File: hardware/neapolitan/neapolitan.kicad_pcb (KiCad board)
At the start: 4 copper layers, 120 x 75 mm, 250 parts, among them J1 USB-MICRO-B, J10 GND_CLIP, J2 RF-SHIELD-FRAME, J3 RF-SHIELD-COVER, J4 MOUNTING_HOLE, J5 MOUNTING_HOLE, J6 MOUNTING_HOLE, J7 MOUNTING_HOLE, J8 MOUNTING_HOLE, J9 MOUNTING_HOLE, P13 GPO1, P14 XCVR_CLKOUT, P15 INTR, P16 CLKIN, P17 GPO6, P18 OEB, P19 GPO3, P2 CLKOUT, P20 GPIO, P21 REF_IN, P22 I2S, P27 MIXER_SDATA, P28 SD, P30 BANK2_AUX, P31 MIXER_SCLK, P32 MIXER_ENX, P33 MIXER_RESETX, P34 MIX_BYPASS, P35 !MIX_BYPASS, P36 VAA, P37 SCL, P38 SDA, P39 SSP1_SCK, P4 ANTENNA, P40 SSP1_MOSI, P41 SSP1_MISO, P42 TX, P43 RX, P44 HP, P45 LP, P46 TX_MIX_BP, P47 RX_MIX_BP, P48 TX_AMP, P49 RX_AMP, P5 LEDS, P50 AMP_BYPASS, P51 !TX_AMP_PWR, P52 !RX_AMP_PWR, P53 CS_XCVR, P55 TXENABLE, P56 RXENABLE, P57 XTAL2, P6 GPO4, P67 RSSI, P7 GPO2, P80 SHIELD, P83 GND, P84 GND, P85 GND, P86 GND, P87 GND, P88 GND, P89 GND, P9 BASEBAND, P90 GND, P91 GND, P92 GND, Q1 MOSFET_P, Q2 MOSFET_P, Q3 MOSFET_P, Q4 MOSFET_P, T1 MIX_IN_BALUN, T2 MIX_OUT_BALUN, T3 RX_BALUN, T4 TX_BALUN, U1 SKY13350, U10 SKY13350, U11 SKY13350, U12 SKY13317, U13 MGA-81563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

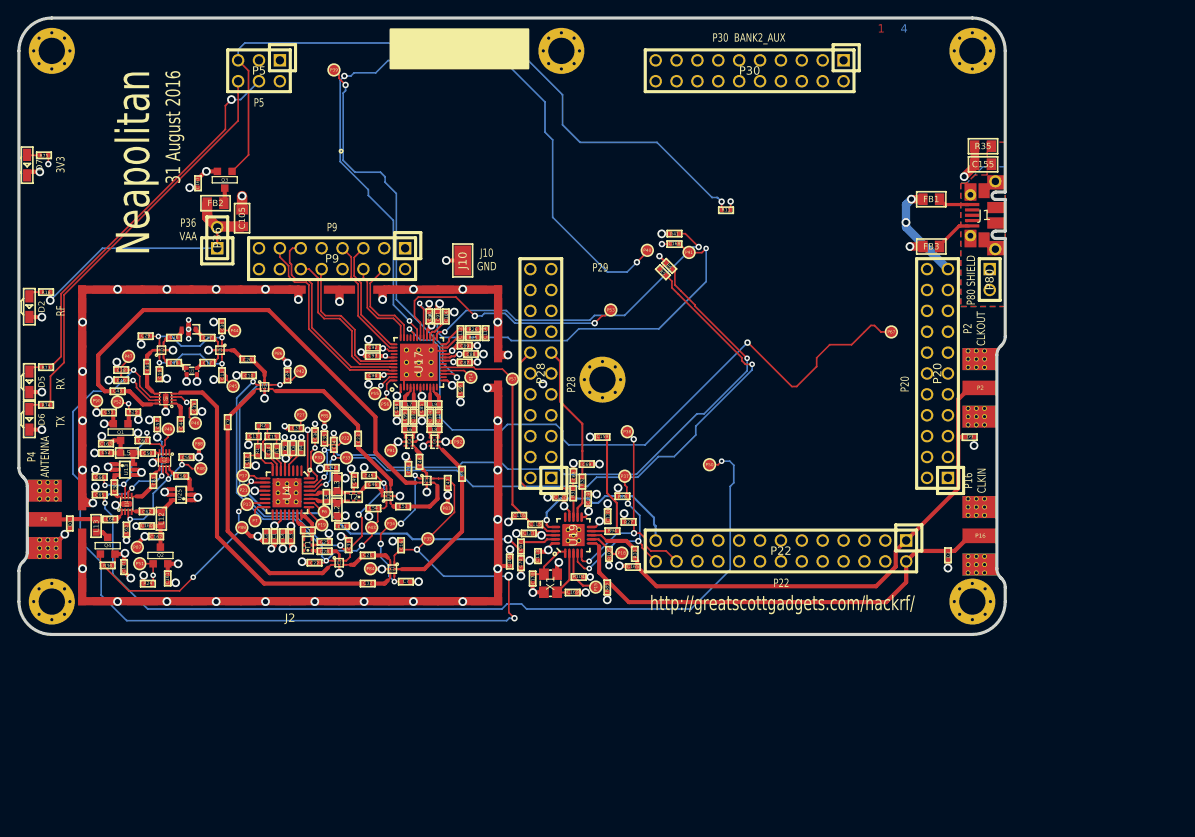
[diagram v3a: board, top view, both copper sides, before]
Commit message: Neapolitan: header pin assignments
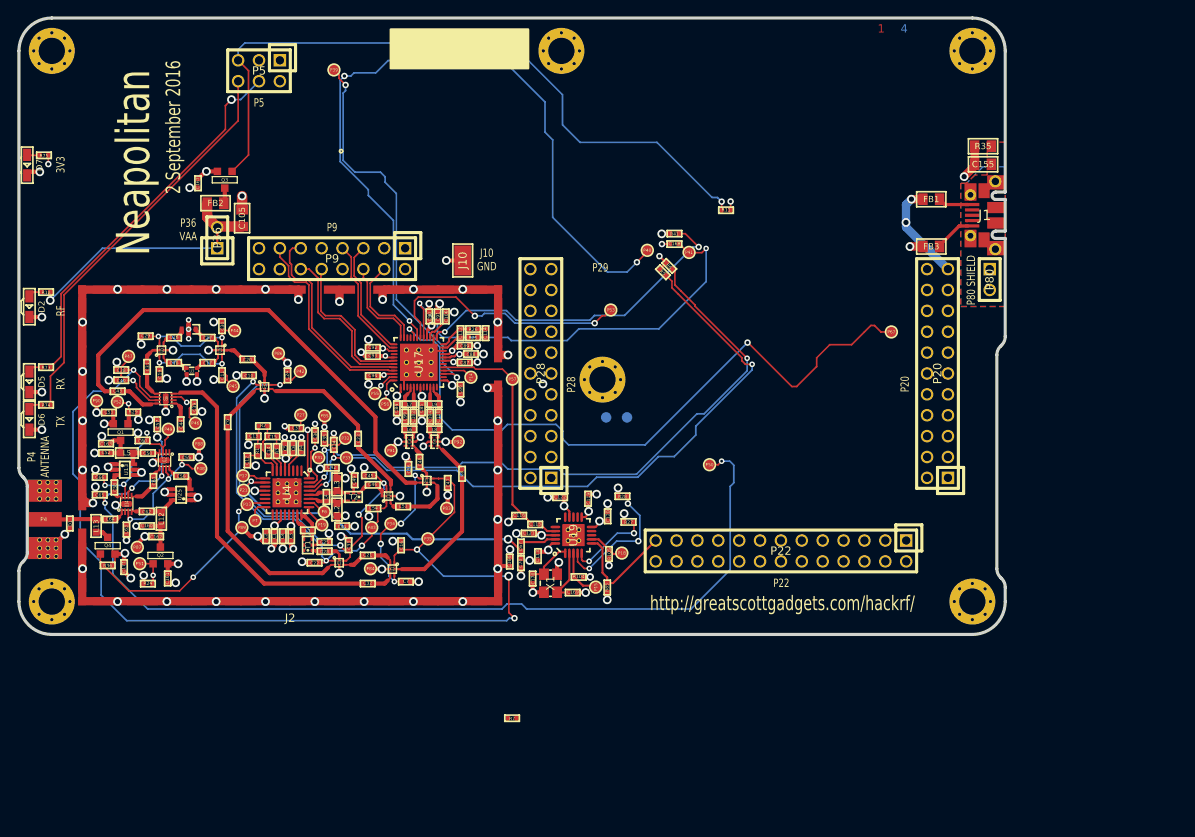
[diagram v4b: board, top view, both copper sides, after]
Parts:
- removed C159, C165, C68, C69: 100pF, hackrf:GSG-0402
- removed D3, D9: GSG-DIODE-TVS-BI, hackrf:GSG-0402
- removed P16: CLKIN, hackrf:GSG-SMA-73251-2120
- removed P2: CLKOUT, hackrf:GSG-SMA-73251-2120
- removed P30: BANK2_AUX, hackrf:GSG-HEADER-2x10
- removed R31, R32, R33, R94: 39, hackrf:GSG-0402
- added R7: 470, hackrf:GSG-0402, F.Cu at (120.0, 185.2)
- P37, P38: moved to B.Cu
- P39: value SSP1_SCK -> SSP0_SCK
- P40: value SSP1_MOSI -> SSP0_MOSI
- P41: value SSP1_MISO -> SSP0_MISO
- moved P37 7.51 mm to (131.4, 148.6)
- moved P38 1.75 mm to (134.0, 148.6)
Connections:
- C168 pad 1: SSP1_MISO -> (no net)
- P20 pad 17: (no net) -> /mcu/usb/power/VBUSCTRL
- P20 pad 18: (no net) -> RSSI
- P22 pad 1: CLKOUT -> (no net)
- P22 pad 2: CLKIN -> (no net)
- P22 pad 5: (no net) -> I2C1_SCL
- P22 pad 6: (no net) -> I2C1_SDA
- P22 pad 7: (no net) -> SSP0_MISO
- P22 pad 8: (no net) -> SSP0_SCK
- P22 pad 9: (no net) -> SSP0_MOSI
- P28 pad 10: (no net) -> XCVR_EN
- P28 pad 13: GCK2 -> (no net)
- P28 pad 14: GCK1 -> (no net)
- P28 pad 4: (no net) -> MIXER_ENX
- P28 pad 5: (no net) -> MIXER_SCLK
- P28 pad 6: (no net) -> MIXER_SDATA
- P28 pad 7: (no net) -> RXENABLE
- P28 pad 8: (no net) -> TXENABLE
- P28 pad 9: (no net) -> CS_XCVR
- P39 pad 1: SSP1_SCK -> SSP0_SCK
- P40 pad 1: SSP1_MOSI -> SSP0_MOSI
- P41 pad 1: SSP1_MISO -> SSP0_MISO
- R27 pad 2: SDA -> I2C1_SDA
- R28 pad 2: SCL -> I2C1_SCL
- R85 pad 1: CLKIN -> CLK6
- U17 pad 15: SSP1_SCK -> SSP0_SCK
- U17 pad 29: SSP1_MISO -> SSP0_MISO
- U17 pad 31: SSP1_MOSI -> SSP0_MOSI
- U19 pad 12: /baseband/CLK1 -> (no net)
- U19 pad 13: /baseband/CLK0 -> (no net)
- U19 pad 16: CLK6 -> (no net)
- U19 pad 4: SCL -> I2C1_SCL
- U19 pad 5: SDA -> I2C1_SDA
- U19 pad 6: CLKIN -> CLK6
- U19 pad 8: /baseband/CLK3 -> (no net)
- U19 pad 9: /baseband/CLK2 -> (no net)
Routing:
- net SSP1_MOSI: track 93.1 -> 0.00 mm, vias 3 -> 0
- net SSP0_MOSI: track 0.00 -> 93.1 mm, vias 0 -> 3
- net CLKOUT: track 62.2 -> 0.00 mm
- net CLKIN: track 58.6 -> 0.00 mm
- net SSP1_MISO: track 52.8 -> 0.00 mm, vias 2 -> 0
- net SSP0_MISO: track 0.00 -> 52.8 mm, vias 0 -> 2
- net SSP1_SCK: track 47.5 -> 0.00 mm, vias 2 -> 0
- net SSP0_SCK: track 0.00 -> 47.5 mm, vias 0 -> 2
- net SDA: track 28.6 -> 0.00 mm, vias 3 -> 0
- net GCK1: track 24.1 -> 0.00 mm
- net SCL: track 22.2 -> 0.00 mm, vias 3 -> 0
- net GCK2: track 16.7 -> 0.00 mm
- net I2C1_SCL: track 0.00 -> 16.3 mm, vias 0 -> 3
- net SGPIO_CLK: track 12.0 -> 0.00 mm
- net I2C1_SDA: track 0.00 -> 10.3 mm, vias 0 -> 2
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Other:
- board text added: "2 September 2016"
- board text removed: "31 August 2016"
- board text removed: "P16 CLKIN"
- board text removed: "P2 CLKOUT"
- board text removed: "P30 BANK2_AUX"

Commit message: Neapolitan: added I/O expander
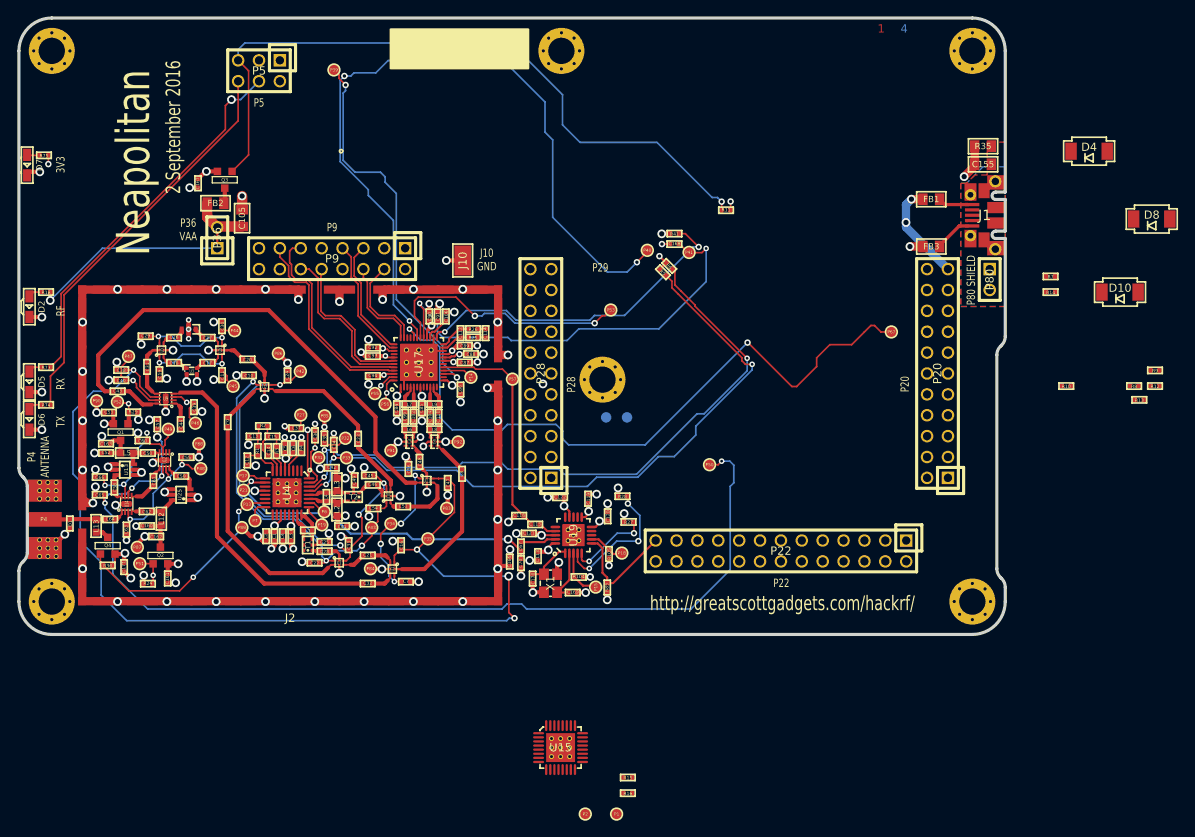
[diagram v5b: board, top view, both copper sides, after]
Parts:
- added D10: VIN_DIODE, gsg-modules:SOD128, F.Cu at (194.0, 133.3)
- added D4: BARREL_DIODE, gsg-modules:SOD128, F.Cu at (190.2, 116.2)
- added D8: VBUS2_DIODE, gsg-modules:SOD128, F.Cu at (197.8, 124.5)
- added P1: !IO_INT, hackrf:GSG-TESTPOINT-50MIL, F.Cu at (132.7, 196.8)
- added P2: !IO_RESET, hackrf:GSG-TESTPOINT-50MIL, F.Cu at (128.9, 196.8)
- added R10: 10k, hackrf:GSG-0402, F.Cu at (187.4, 144.8)
- added R12: 18k, hackrf:GSG-0402, F.Cu at (198.2, 144.8)
- added R13: 10k, hackrf:GSG-0402, F.Cu at (196.3, 146.5)
- added R14: 18k, hackrf:GSG-0402, F.Cu at (185.5, 133.3)
- added R15: 10k, hackrf:GSG-0402, F.Cu at (134.1, 192.4)
- added R16: 10k, hackrf:GSG-0402, F.Cu at (134.1, 194.3)
- added R8: 10k, hackrf:GSG-0402, F.Cu at (195.7, 144.8)
- added R9: 18k, hackrf:GSG-0402, F.Cu at (198.2, 142.9)
- added U15: TCA6424A, gsg-modules:QFN32-5, F.Cu at (125.9, 188.8)
- moved R7 84.7 mm to (185.5, 131.4)
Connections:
- FB1 pad 2: (no net) -> /mcu/usb/power/VBUS2
- P20 pad 21: (no net) -> /mcu/usb/power/VBUS
- P20 pad 22: (no net) -> /mcu/usb/power/VIN
- P22 pad 24: SDA -> (no net)
- P22 pad 26: SCL -> (no net)
- P37 pad 1: SCL -> (no net)
- P38 pad 1: SDA -> (no net)
- R7 pad 1: (no net) -> Net-(D10-Pad2)
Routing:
- net (no net): track 20.8 -> 8.48 mm, vias 2 -> 0
- net /mcu/usb/power/VBUS: track 0.00 -> 7.22 mm
- net /mcu/usb/power/VBUS2: track 0.00 -> 5.08 mm, vias 0 -> 2

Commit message: Neapolitan: barrel jack module
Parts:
- added J11: BARREL_JACK, gsg-modules:CUI_PJ-102[AB]H, F.Cu at (169.3, 111.8)
- moved R35 20.9 mm to (177.0, 136.5)
- moved C155 20.9 mm to (177.0, 138.7)
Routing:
- net /mcu/usb/power/VBUS: track 7.22 -> 9.96 mm, vias 0 -> 1
- net /mcu/usb/power/VBUS2: track 5.08 -> 2.34 mm, vias 2 -> 1
- net GND: track 396.4 -> 397.5 mm, vias 136 -> 135
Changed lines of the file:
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@@
 (kicad_pcb (version 4) (host pcbnew "(2015-08-18 BZR 6102)-product")
   (general
-    (links 697)
-    (no_connects 55)
+    (links 699)
+    (no_connects 64)
     (area 59.329499 99.809499 180.670501 175.190501)
     (thickness 1.6002)
     (drawings 71)
-    (tracks 1726)
+    (tracks 1725)
     (zones 0)
-    (modules 252)
+    (modules 253)
     (nets 151)
   )
@@
   )
   (setup
-    (last_trace_width 0.254)
+    (last_trace_width 1.27)
     (user_trace_width 0.1524)
     (user_trace_width 0.2032)
@@
   )
   (module hackrf:GSG-0805 (layer C1F)
-    (at 177.3 117.8 180)
+    (at 177 138.7 180)
     (solder_mask_margin 0.1016)
     (fp_text reference C155 (at 0 0 180) (layer F.SilkS)
@@
   )
   (module hackrf:GSG-0805 (layer C1F)
-    (at 177.3 115.6 180)
+    (at 177 136.5 180)
     (solder_mask_margin 0.1016)
     (fp_text reference R35 (at 0 0 180) (layer F.SilkS)
@@
       (net 146 /mcu/usb/power/!IO_INT))
   )
+  (module gsg-modules:CUI_PJ-102[AB]H (layer C1F)
+    (at 169.3 111.8 270)
+    (fp_text reference J11 (at 0 0 270) (layer F.SilkS)
+      (effects (font (thickness 0.3048)))
+    )
+    (fp_text value BARREL_JACK (at 0 0 270) (layer F.SilkS) hide
+      (effects (font (thickness 0.3048)))
+    )
+    (fp_line (start -4.5 -10.7) (end 4.5 -10.7) (layer F.SilkS) (width 0.2032))
+    (fp_line (start 4.5 -10.7) (end 4.5 3.7) (layer F.SilkS) (width 0.2032))
+    (fp_line (start 4.5 3.7) (end -4.5 3.7) (layer F.SilkS) (width 0.2032))
+    (fp_line (start -4.5 3.7) (end -4.5 -10.7) (layer F.SilkS) (width 0.2032))
+    (pad 1 thru_hole circle (at 0 3 270) (size 3 3) (drill 1.5) (layers *.Cu *.Mask F.SilkS)
+      (net 144 /mcu/usb/power/BARREL))
+    (pad 2 thru_hole circle (at 0 -3 270) (size 3 3) (drill 1.5) (layers *.Cu *.Mask F.SilkS)
+      (net 33 GND))
+    (pad 3 thru_hole circle (at -4.7 0 270) (size 3 3) (drill 1.5) (layers *.Cu *.Mask F.SilkS))
+    (pad "" np_thru_hole circle (at 0 -7.5 270) (size 2.2 2.2) (drill 2.2) (layers *.Cu *.Mask F.SilkS))
+  )
   (gr_line (start 180 126.825) (end 180 138.74) (angle 90) (layer Edge.Cuts) (width 0.381))
   (gr_line (start 180 122.075) (end 180 125.925) (angle 90) (layer Edge.Cuts) (width 0.381))
@@
   (segment (start 115.4542 136.2456) (end 115.4684 136.2456) (width 0.2032) (layer C1F) (net 32))
   (segment (start 120.344302 137.1286) (end 130.0532 137.1286) (width 0.2032) (layer C4B) (net 32))
+  (segment (start 173.03 138.17) (end 175.454 138.17) (width 1.27) (layer C1F) (net 33))
+  (segment (start 175.454 138.17) (end 175.984 138.7) (width 1.27) (layer C1F) (net 33))
+  (segment (start 175.984 136.5) (end 175.984 138.7) (width 1.27) (layer C1F) (net 33))
   (segment (start 94.5762 166.2726) (end 94.4492 166.1456) (width 0.508) (layer C1F) (net 33))
   (segment (start 75.0176 161.81) (end 74.2556 161.81) (width 0.508) (layer C1F) (net 33) (status 10))
@@
   (via (at 168.4072 127.8068) (size 1.0668) (drill 0.635) (layers C1F C4B) (net 33))
   (segment (start 169.984 127.8) (end 168.414 127.8) (width 1.016) (layer C1F) (net 33) (status 10))
-  (segment (start 176.284 115.6) (end 176.284 117.8) (width 1.016) (layer C1F) (net 33) (status 30))
-  (segment (start 176.284 117.8) (end 176.284 118.016) (width 1.016) (layer C1F) (net 33) (status 30))
-  (segment (start 176.284 118.016) (end 175 119.3) (width 1.016) (layer C1F) (net 33) (status 10))
-  (via (at 175 119.3) (size 1.0668) (drill 0.635) (layers C1F C4B) (net 33))
   (segment (start 61.2754 145.5106) (end 62.794 145.5106) (width 0.508) (layer C1F) (net 33) (status 10))
   (via (at 62.794 145.5106) (size 1.0668) (drill 0.635) (layers C1F C4B) (net 33))
@@
   (segment (start 135.18654 129.71434) (end 136.454 128.44688) (width 0.2032) (layer C1F) (net 140) (status 20))
   (segment (start 173.03 130.55) (end 167.925 125.445) (width 1.016) (layer C4B) (net 141) (status 10))
+  (segment (start 167.925 125.445) (end 167.925 124.875) (width 1.016) (layer C4B) (net 141))
+  (segment (start 167.925 122.701) (end 167.925 124.875) (width 1.016) (layer C4B) (net 141))
+  (via (at 167.925 124.875) (size 1.0668) (drill 0.635) (layers C1F C4B) (net 141))
   (segment (start 168.594 122.05) (end 168.585 122.041) (width 1.016) (layer C1F) (net 145))
   (via (at 168.585 122.041) (size 1.0668) (drill 0.635) (layers C1F C4B) (net 145))
   (segment (start 168.585 122.041) (end 167.925 122.701) (width 1.016) (layer C4B) (net 145))
-  (segment (start 167.925 122.701) (end 167.925 124.875) (width 1.016) (layer C4B) (net 145))
-  (via (at 167.925 124.875) (size 1.0668) (drill 0.635) (layers C1F C4B) (net 145))
   (segment (start 169.984 122.05) (end 168.594 122.05) (width 1.016) (layer C1F) (net 145) (status 10))
-  (segment (start 167.925 125.445) (end 167.925 124.875) (width 1.016) (layer C4B) (net 145))
   (zone (net 0) (net_name "") (layer F.SilkS) (hatch edge 0.508)
     (connect_pads (clearance 0.3048))
